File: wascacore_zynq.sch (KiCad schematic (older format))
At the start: 50 parts, among them U1 DDR3, U2 xc7z010clg400

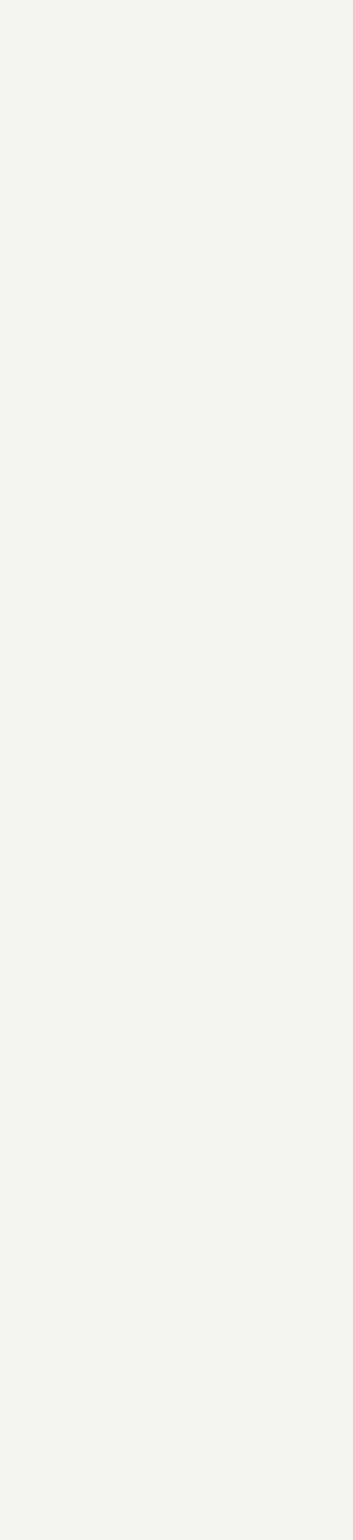
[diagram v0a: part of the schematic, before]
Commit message: Components and layout import
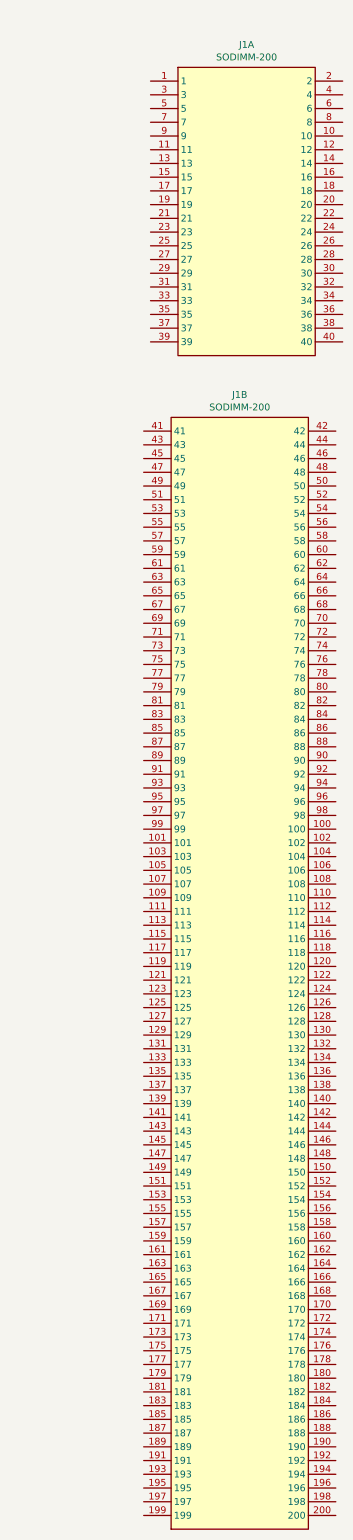
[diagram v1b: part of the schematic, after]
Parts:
- added J1: SODIMM-200, SODIMM:SODIMM_DDR2_EDGE, symbol Connector:SODIMM-200
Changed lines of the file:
@@
 EELAYER 30 0
 EELAYER END
-$Descr A4 8268 11693 portrait
+$Descr A2 23386 16535
 encoding utf-8
 Sheet 1 1
@@
 Connection ~ 1300 4300
 Connection ~ 1300 4950
+$Comp
+L Connector:SODIMM-200 J1
+U 1 1 61BB8D12
+P 11100 2050
+F 0 "J1" H 11100 3215 50  0000 C CNN
+F 1 "SODIMM-200" H 11100 3124 50  0000 C CNN
+F 2 "SODIMM:SODIMM_DDR2_EDGE" H 12500 5900 50  0001 C CNN
+F 3 "~" H 12500 5900 50  0001 C CNN
+	1    11100 2050
+	1    0    0    -1
+$EndComp
+$Comp
+L Connector:SODIMM-200 J1
+U 2 1 61BBE4B4
+P 11050 7600
+F 0 "J1" H 11050 11765 50  0000 C CNN
+F 1 "SODIMM-200" H 11050 11674 50  0000 C CNN
+F 2 "SODIMM:SODIMM_DDR2_EDGE" H 12450 11450 50  0001 C CNN
+F 3 "~" H 12450 11450 50  0001 C CNN
+	2    11050 7600
+	1    0    0    -1
+$EndComp
 $EndSCHEMATC

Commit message: SDRAM added
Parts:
- added IC1: SDRAM_MT48_x16, Package_SO:TSOP-II-54_22.2x10.16mm_P0.8mm, symbol wasca:SDRAM_MT48_x16
- added unit 1 of U2
- added unit 2 of U2
- added unit 3 of U2
- added unit 4 of U2
- added unit 5 of U2
- added unit 6 of U2
- added unit 9 of U2
- U2: footprint Package_BGA:Xilinx_CLG400_NoPaste_JLC_Package_Delay -> (none)
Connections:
- new net: U2.T8 (VCCO_13[4]), U2.U11 (VCCO_13[4]), U2.W7 (VCCO_13[4]), U2.Y10 (VCCO_13[4])
- new net: U2.N19 (VCCO_34[6]), U2.R15 (VCCO_34[6]), U2.T18 (VCCO_34[6]), U2.V14 (VCCO_34[6]), U2.W17 (VCCO_34[6]), U2.Y20 (VCCO_34[6])
- new net: U2.C19 (VCCO_35[6]), U2.F18 (VCCO_35[6]), U2.H14 (VCCO_35[6]), U2.J17 (VCCO_35[6]), U2.K20 (VCCO_35[6]), U2.M16 (VCCO_35[6])
- new net: U2.B6 (VCCO_MIO0_500[2]), U2.D7 (VCCO_MIO0_500[2])
- new net: U2.A13 (VCCO_MIO1_501[4]), U2.B16 (VCCO_MIO1_501[4]), U2.D12 (VCCO_MIO1_501[4]), U2.E15 (VCCO_MIO1_501[4])
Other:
- moved on the sheet: J1A, J1B, U2H
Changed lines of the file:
@@
 F 0 "U2" H 6450 1100 60  0000 L CNN
 F 1 "xc7z010clg400" H 6700 1100 60  0000 L CNN
-F 2 "Package_BGA:Xilinx_CLG400_NoPaste_JLC_Package_Delay" H 6450 950 60  0001 L CNN
+F 2 "" H 6450 950 60  0001 L CNN
 F 3 "" H 6450 750 60  0001 L CNN
 F 4 "xc7z010clg400" H 6450 650 60  0001 L CNN "desc"
@@
 L 7z010_ddr:xc7z010clg400 U2
 U 8 1 619FCFE9
-P 6250 8600
-F 0 "U2" H 7080 8353 60  0000 L CNN
-F 1 "xc7z010clg400" H 7080 8247 60  0000 L CNN
-F 2 "Package_BGA:Xilinx_CLG400_NoPaste_JLC_Package_Delay" H 6450 8650 60  0001 L CNN
-F 3 "" H 6450 8450 60  0001 L CNN
-F 4 "xc7z010clg400" H 6450 8350 60  0001 L CNN "desc"
-	8    6250 8600
+P 6250 9100
+F 0 "U2" H 7080 8853 60  0000 L CNN
+F 1 "xc7z010clg400" H 7080 8747 60  0000 L CNN
+F 2 "" H 6450 9150 60  0001 L CNN
+F 3 "" H 6450 8950 60  0001 L CNN
+F 4 "xc7z010clg400" H 6450 8850 60  0001 L CNN "desc"
+	8    6250 9100
 	1    0    0    -1
 $EndComp
@@
 L power:GND #PWR0101
 U 1 1 61A0FC06
-P 6250 8600
-F 0 "#PWR0101" H 6250 8350 50  0001 C CNN
-F 1 "GND" V 6255 8472 50  0000 R CNN
-F 2 "" H 6250 8600 50  0001 C CNN
-F 3 "" H 6250 8600 50  0001 C CNN
-	1    6250 8600
+P 6250 9100
+F 0 "#PWR0101" H 6250 8850 50  0001 C CNN
+F 1 "GND" V 6255 8972 50  0000 R CNN
+F 2 "" H 6250 9100 50  0001 C CNN
+F 3 "" H 6250 9100 50  0001 C CNN
+	1    6250 9100
 	0    1    1    0
 $EndComp
-NoConn ~ 6250 8700
-NoConn ~ 6250 8800
-NoConn ~ 6250 8900
-NoConn ~ 6250 9000
-NoConn ~ 6250 9100
 NoConn ~ 6250 9200
+NoConn ~ 6250 9300
+NoConn ~ 6250 9400
+NoConn ~ 6250 9500
+NoConn ~ 6250 9600
+NoConn ~ 6250 9700
 Connection ~ 3150 1900
 Connection ~ 2650 1900
@@
 L Connector:SODIMM-200 J1
 U 1 1 61BB8D12
-P 11100 2050
-F 0 "J1" H 11100 3215 50  0000 C CNN
-F 1 "SODIMM-200" H 11100 3124 50  0000 C CNN
-F 2 "SODIMM:SODIMM_DDR2_EDGE" H 12500 5900 50  0001 C CNN
-F 3 "~" H 12500 5900 50  0001 C CNN
-	1    11100 2050
+P 21500 2500
+F 0 "J1" H 21500 3665 50  0000 C CNN
+F 1 "SODIMM-200" H 21500 3574 50  0000 C CNN
+F 2 "SODIMM:SODIMM_DDR2_EDGE" H 22900 6350 50  0001 C CNN
+F 3 "~" H 22900 6350 50  0001 C CNN
+	1    21500 2500
 	1    0    0    -1
 $EndComp
@@
 L Connector:SODIMM-200 J1
 U 2 1 61BBE4B4
-P 11050 7600
-F 0 "J1" H 11050 11765 50  0000 C CNN
-F 1 "SODIMM-200" H 11050 11674 50  0000 C CNN
-F 2 "SODIMM:SODIMM_DDR2_EDGE" H 12450 11450 50  0001 C CNN
-F 3 "~" H 12450 11450 50  0001 C CNN
-	2    11050 7600
-	1    0    0    -1
-$EndComp
+P 21450 8050
+F 0 "J1" H 21450 12215 50  0000 C CNN
+F 1 "SODIMM-200" H 21450 12124 50  0000 C CNN
+F 2 "SODIMM:SODIMM_DDR2_EDGE" H 22850 11900 50  0001 C CNN
+F 3 "~" H 22850 11900 50  0001 C CNN
+	2    21450 8050
+	1    0    0    -1
+$EndComp
+$Comp
+L 7z010_ddr:xc7z010clg400 U2
+U 1 1 61C45AD7
+P 10200 950
+F 0 "U2" H 11130 -47 60  0000 L CNN
+F 1 "xc7z010clg400" H 11130 -153 60  0000 L CNN
+F 2 "" H 10400 1000 60  0001 L CNN
+F 3 "" H 10400 800 60  0001 L CNN
+F 4 "xc7z010clg400" H 10400 700 60  0001 L CNN "desc"
+	1    10200 950
+	1    0    0    -1
+$EndComp
+$Comp
+L 7z010_ddr:xc7z010clg400 U2
+U 2 1 61C54027
+P 10400 3650
+F 0 "U2" H 10793 3940 60  0000 C CNN
+F 1 "xc7z010clg400" H 10793 3834 60  0000 C CNN
+F 2 "" H 10600 3700 60  0001 L CNN
+F 3 "" H 10600 3500 60  0001 L CNN
+F 4 "xc7z010clg400" H 10600 3400 60  0001 L CNN "desc"
+	2    10400 3650
+	1    0    0    -1
+$EndComp
+$Comp
+L 7z010_ddr:xc7z010clg400 U2
+U 3 1 61C621BA
+P 9900 4250
+F 0 "U2" H 11430 1803 60  0000 L CNN
+F 1 "xc7z010clg400" H 11430 1697 60  0000 L CNN
+F 2 "" H 10100 4300 60  0001 L CNN
+F 3 "" H 10100 4100 60  0001 L CNN
+F 4 "xc7z010clg400" H 10100 4000 60  0001 L CNN "desc"
+	3    9900 4250
+	1    0    0    -1
+$EndComp
+$Comp
+L 7z010_ddr:xc7z010clg400 U2
+U 4 1 61C717CA
+P 12600 4300
+F 0 "U2" H 14130 1853 60  0000 L CNN
+F 1 "xc7z010clg400" H 14130 1747 60  0000 L CNN
+F 2 "" H 12800 4350 60  0001 L CNN
+F 3 "" H 12800 4150 60  0001 L CNN
+F 4 "xc7z010clg400" H 12800 4050 60  0001 L CNN "desc"
+	4    12600 4300
+	1    0    0    -1
+$EndComp
+$Comp
+L 7z010_ddr:xc7z010clg400 U2
+U 5 1 61C8D9E7
+P 9450 10250
+F 0 "U2" H 10580 9403 60  0000 L CNN
+F 1 "xc7z010clg400" H 10580 9297 60  0000 L CNN
+F 2 "" H 9650 10300 60  0001 L CNN
+F 3 "" H 9650 10100 60  0001 L CNN
+F 4 "xc7z010clg400" H 9650 10000 60  0001 L CNN "desc"
+	5    9450 10250
+	1    0    0    -1
+$EndComp
+$Comp
+L 7z010_ddr:xc7z010clg400 U2
+U 6 1 61C9EFD0
+P 12850 9850
+F 0 "U2" H 13980 7903 60  0000 L CNN
+F 1 "xc7z010clg400" H 13980 7797 60  0000 L CNN
+F 2 "" H 13050 9900 60  0001 L CNN
+F 3 "" H 13050 9700 60  0001 L CNN
+F 4 "xc7z010clg400" H 13050 9600 60  0001 L CNN "desc"
+	6    12850 9850
+	1    0    0    -1
+$EndComp
+$Comp
+L 7z010_ddr:xc7z010clg400 U2
+U 9 1 61CAE983
+P 15400 8850
+F 0 "U2" H 15830 7703 60  0000 L CNN
+F 1 "xc7z010clg400" H 15830 7597 60  0000 L CNN
+F 2 "" H 15600 8900 60  0001 L CNN
+F 3 "" H 15600 8700 60  0001 L CNN
+F 4 "xc7z010clg400" H 15600 8600 60  0001 L CNN "desc"
+	9    15400 8850
+	1    0    0    -1
+$EndComp
+$Comp
+L wasca:SDRAM_MT48_x16 IC1
+U 1 1 61D1F0C2
+P 17350 3200
+F 0 "IC1" H 17350 4864 40  0000 C CNN
+F 1 "SDRAM_MT48_x16" H 17350 4788 40  0000 C CNN
+F 2 "Package_SO:TSOP-II-54_22.2x10.16mm_P0.8mm" H 17350 4697 60  0000 C CNN
+F 3 "" H 17350 3200 60  0000 C CNN
+	1    17350 3200
+	1    0    0    -1
+$EndComp

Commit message: Routing from wasca board
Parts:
- added C1, C2, C21, C23, C42, C43, C44, C45, C46, C47, C48, C49, C51, C52, C53, C54, C56, C57, C58, C59, C60, C61, C62, C63, C64, C65, C66, C67, C68, C69, C70, C71, C72, C73: 0.1uF, Capacitor_SMD:C_0603_1608Metric_Pad1.05x0.95mm_HandSolder, symbol Device:C_Small
- added C50: 10uF, Capacitors_SMD:C_1206_HandSoldering, symbol Device:C_Small
- added C55: 4.7uF, Capacitor_SMD:C_0603_1608Metric_Pad1.05x0.95mm_HandSolder, symbol Device:C_Small
- added CN1, CN3: Conn_02x02_Odd_Even, Connector_PinHeader_2.54mm:PinHeader_2x02_P2.54mm_Vertical, symbol Connector_Generic:Conn_02x02_Odd_Even
- added CN2: Conn_02x05_Odd_Even, wasca:Multicomp_MC9A22-1034_2x05_P2.54mm_Horizontal, symbol Connector_Generic:Conn_02x05_Odd_Even
- added CN4: Conn_02x03_Odd_Even, Connector_PinHeader_2.54mm:PinHeader_2x03_P2.54mm_Vertical, symbol Connector_Generic:Conn_02x03_Odd_Even
- added CN5: USB_C_Receptacle_USB2.0, wasca:DX07S016JA1R1500, symbol Connector:USB_C_Receptacle_USB2.0
- added D1: LED_RGB, LED_SMD:LED_RGB_5050-6, symbol Device:LED_RGB
- added D2: LED_BCGR, LED_THT:LED_D5.0mm-4_RGB, symbol Device:LED_BCGR
- added D3: LED, LED_THT:LED_D3.0mm, symbol Device:LED
- added D4: BAT54C, Package_TO_SOT_SMD:SOT-23, symbol Diode:BAT54C
- added R1: 1K, Capacitor_SMD:C_0603_1608Metric_Pad1.05x0.95mm_HandSolder, symbol Device:R
- added R10, R11, R8, R9: 470, Capacitor_SMD:C_0603_1608Metric_Pad1.08x0.95mm_HandSolder, symbol Device:R
- added R14: 470, Capacitor_SMD:C_0603_1608Metric_Pad1.05x0.95mm_HandSolder, symbol Device:R
- added R15: 5K1, Capacitor_SMD:C_0603_1608Metric_Pad1.08x0.95mm_HandSolder, symbol Device:R
- added R16: 4K7, Capacitor_SMD:C_0603_1608Metric_Pad1.05x0.95mm_HandSolder, symbol Device:R
- added R17, R3, R4: 10K, Capacitor_SMD:C_0603_1608Metric_Pad1.05x0.95mm_HandSolder, symbol Device:R
- added R2: 0, Capacitor_SMD:C_0603_1608Metric_Pad1.08x0.95mm_HandSolder, symbol Device:R
- added U1, U2, U5, U6, U7: SN74LVC1T45DBV, Package_TO_SOT_SMD:SOT-23-6, symbol Logic_LevelTranslator:SN74LVC1T45DBV
- added U8: LD1117S33TR_SOT223, Package_TO_SOT_SMD:SOT-223-3_TabPin2, symbol Regulator_Linear:LD1117S33TR_SOT223
- renumbered C8 to C10, C9 to C11, C10 to C12, C11 to C13, C12 to C14, C13 to C15, C14 to C16, C15 to C17, C16 to C18, C17 to C19, C18 to C20, C19 to C22, C20 to C24, C21 to C25, C22 to C26, C23 to C27, C24 to C28, C25 to C29, C1 to C3, C26 to C30, C27 to C31, C28 to C32, C29 to C33, C30 to C34, C31 to C35, C32 to C36, C33 to C37, C34 to C38, C35 to C39, C2 to C4, C36 to C40, C37 to C41, C3 to C5, C4 to C6, C5 to C7, C6 to C8, C7 to C9, R4 to R12, R5 to R13, R1 to R5, R2 to R6, R3 to R7, U1 to U3, U2 to U4
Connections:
- net labels added: +3_3V, +5V_SATURN, +5V_SYS, +5V_USB, 5V, 5V_SATURN_DETECT, ABUS_3V_A1, ABUS_3V_A10, ABUS_3V_A11, ABUS_3V_A12, ABUS_3V_A13, ABUS_3V_A14, ABUS_3V_A15, ABUS_3V_A16, ABUS_3V_A17, ABUS_3V_A18, ABUS_3V_A19, ABUS_3V_A2, ABUS_3V_A20, ABUS_3V_A21, ABUS_3V_A22, ABUS_3V_A23, ABUS_3V_A24, ABUS_3V_A3, ABUS_3V_A4, ABUS_3V_A5, ABUS_3V_A6, ABUS_3V_A7, ABUS_3V_A8, ABUS_3V_A9, ABUS_3V_CS0, ABUS_3V_CS1, ABUS_3V_CS2, ABUS_3V_D0, ABUS_3V_D1, ABUS_3V_D10, ABUS_3V_D11, ABUS_3V_D12, ABUS_3V_D13, ABUS_3V_D14, ABUS_3V_D15, ABUS_3V_D2, ABUS_3V_D3, ABUS_3V_D4, ABUS_3V_D5, ABUS_3V_D6, ABUS_3V_D7, ABUS_3V_D8, ABUS_3V_D9, ABUS_3V_IRQ, ABUS_3V_MUX_DATA_DIR, ABUS_3V_RD, ABUS_3V_WR0, ABUS_3V_WR1, ABUS_IRQ, BUFFERS_OE, BUFFSPI_CS, BUFFSPI_MISO, BUFFSPI_MOSI, BUFFSPI_SCK, BUFFSPI_SYNC, DBG_UART_RX, DBG_UART_TX, ESP32_CS, ESP32_MISO, ESP32_MOSI, ESP32_SCK, FPGA_60MHZ, IBCK, IBCK_3V, ILRCK, ILRCK_3V, IRQ_OUT_ENABLE, ISD, ISD_3V, JTAG_TCK, JTAG_TDI, JTAG_TDO, JTAG_TMS, LED3, LEDB, LEDG, LEDR, RESET_3V, SCSPCLK, SDR_A0, SDR_A1, SDR_A10, SDR_A11, SDR_A12, SDR_A2, SDR_A3, SDR_A4, SDR_A5, SDR_A6, SDR_A7, SDR_A8, SDR_A9, SDR_BA0, SDR_BA1, SDR_CAS, SDR_CKE, SDR_CLK, SDR_CS, SDR_DQ0, SDR_DQ1, SDR_DQ10, SDR_DQ11, SDR_DQ12, SDR_DQ13, SDR_DQ14, SDR_DQ15, SDR_DQ2, SDR_DQ3, SDR_DQ4, SDR_DQ5, SDR_DQ6, SDR_DQ7, SDR_DQ8, SDR_DQ9, SDR_DQMH, SDR_DQML, SDR_RAS, SDR_WE, SD_CLK, SD_CMD, SD_DAT0, SD_DAT1, SD_DAT2, SD_DAT3, SD_DET_A, SD_DET_B, SSEL, SSEL_3V, SWCLK, SWDIO, USB_DM, USB_DP, VBUS_SENSE, VCC_SDRAM
- wire segments 130 -> 643
- no-connect marks 28 -> 32
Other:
- note added: "5V Tolerant pin"
- note added: "Compatible connectors:\nJAE DX07S016JA1R1500\nJAE DX07S016JA3R1500\nHROPARTS TYPE-C-31-M-12\nHROPARTS TYPE-C-31-M-14\nXKB U262-161N-4BVC11\nJing Ext. C167321"
- note added: "External 5V power supply\n+ 3V3 power output/check"
- note added: "ONLY 1 OF THE RGB LEDS SHOULD BE PLACED"
- note added: "SDRAM : shares 3V3 with MAX10\nDDR : requires 2V5 power supply"
- moved on the sheet: C10, C11, C12, C13, C14, C15, C16, C17, C18, C19, C20, C22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
